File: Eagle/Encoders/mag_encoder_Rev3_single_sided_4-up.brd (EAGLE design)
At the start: 10 x 24 mm, 5 parts, among them IC1 A1203LH

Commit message: Updated ecoder gcode again...
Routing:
- net VCC: track 33.2 -> 36.7 mm
- net SIG: track 22.0 -> 24.4 mm
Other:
- board size 10 x 24 mm -> 12.9 x 24 mm
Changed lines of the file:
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@@
 <text x="11.8225" y="18.705" size="0.762" layer="25">SIG</text>
 <text x="8.838" y="18.705" size="0.762" layer="25">VCC</text>
-<wire x1="4.75" y1="1.5" x2="4.75" y2="25.5" width="0" layer="20"/>
-<wire x1="14.75" y1="25.5" x2="14.75" y2="1.5" width="0" layer="20"/>
-<wire x1="14.75" y1="1.5" x2="4.75" y2="1.5" width="0" layer="20"/>
-<wire x1="4.75" y1="25.5" x2="14.75" y2="25.5" width="0" layer="20"/>
+<wire x1="3.125" y1="1.5" x2="3.125" y2="25.5" width="0.01" layer="20"/>
+<wire x1="16" y1="25.5" x2="16" y2="1.5" width="0.01" layer="20"/>
+<wire x1="16" y1="1.5" x2="3.125" y2="1.5" width="0.01" layer="20"/>
+<wire x1="3.125" y1="25.5" x2="16" y2="25.5" width="0.01" layer="20"/>
 </plain>
 <attributes>
@@
 <contactref element="C1" pad="2"/>
 <contactref element="U$1" pad="P$3"/>
-<wire x1="12.375" y1="11.125" x2="9.875" y2="11.125" width="0.635" layer="1"/>
-<wire x1="9.875" y1="11.125" x2="7.75" y2="11.125" width="0.635" layer="1"/>
 <wire x1="7.75" y1="11.125" x2="7.667" y2="11.04" width="0.635" layer="1"/>
 <wire x1="12.375" y1="11.125" x2="12.412" y2="11.04" width="0.635" layer="1"/>
-<wire x1="9.875" y1="11.125" x2="9.875" y2="6.125" width="0.635" layer="1"/>
 <wire x1="9.875" y1="6.125" x2="9.852" y2="6.115" width="0.635" layer="1"/>
-<wire x1="7.375" y1="11.125" x2="7.375" y2="22" width="0.635" layer="1"/>
 <wire x1="7.375" y1="22" x2="7.2935" y2="22.0995" width="0.635" layer="1"/>
 <wire x1="7.375" y1="11.125" x2="7.667" y2="11.04" width="0.635" layer="1"/>
 <polygon width="0.4064" layer="1" thermals="no">
-<vertex x="-1" y="30.875"/>
-<vertex x="20.125" y="30.875"/>
-<vertex x="20.125" y="0.25"/>
-<vertex x="-0.625" y="0.25"/>
+<vertex x="2.125" y="26"/>
+<vertex x="16.625" y="26"/>
+<vertex x="16.625" y="0.25"/>
+<vertex x="2.25" y="0.25"/>
 </polygon>
+<wire x1="9.875" y1="6.125" x2="9.875" y2="10.25" width="1.016" layer="1"/>
+<wire x1="9.875" y1="10.25" x2="10.665" y2="11.04" width="1.016" layer="1"/>
+<wire x1="10.665" y1="11.04" x2="12.412" y2="11.04" width="1.016" layer="1"/>
+<wire x1="9.875" y1="10.25" x2="9.085" y2="11.04" width="1.016" layer="1"/>
+<wire x1="9.085" y1="11.04" x2="7.667" y2="11.04" width="1.016" layer="1"/>
+<wire x1="7.375" y1="11.125" x2="7.375" y2="22.018" width="1.016" layer="1"/>
+<wire x1="7.375" y1="22.018" x2="7.2935" y2="22.0995" width="1.016" layer="1"/>
 </signal>
 <signal name="VCC">
@@
 <contactref element="R1" pad="2"/>
 <contactref element="U$1" pad="P$2"/>
-<wire x1="7.75" y1="4.625" x2="7.75" y2="9.25" width="0.635" layer="1"/>
-<wire x1="8.75" y1="3.625" x2="7.75" y2="4.625" width="0.635" layer="1"/>
 <wire x1="7.75" y1="9.25" x2="7.667" y2="9.34" width="0.635" layer="1"/>
 <wire x1="8.75" y1="3.625" x2="8.752" y2="3.515" width="0.635" layer="1"/>
-<wire x1="9.375" y1="21.625" x2="9.375" y2="15.75" width="0.635" layer="1"/>
-<wire x1="9.75" y1="22" x2="9.375" y2="21.625" width="0.635" layer="1"/>
-<wire x1="9.375" y1="15.75" x2="9.252" y2="15.63" width="0.635" layer="1"/>
-<wire x1="9.75" y1="22" x2="9.7935" y2="22.0995" width="0.635" layer="1"/>
-<wire x1="6.75" y1="9.5" x2="7.375" y2="9.5" width="0.635" layer="1"/>
-<wire x1="5.625" y1="10.625" x2="6.75" y2="9.5" width="0.635" layer="1"/>
-<wire x1="5.625" y1="23" x2="5.625" y2="10.625" width="0.635" layer="1"/>
-<wire x1="6.375" y1="23.75" x2="5.625" y2="23" width="0.635" layer="1"/>
-<wire x1="8.375" y1="23.75" x2="6.375" y2="23.75" width="0.635" layer="1"/>
-<wire x1="9.75" y1="22.375" x2="8.375" y2="23.75" width="0.635" layer="1"/>
-<wire x1="7.375" y1="9.5" x2="7.667" y2="9.34" width="0.635" layer="1"/>
 <wire x1="9.75" y1="22.375" x2="9.7935" y2="22.0995" width="0.635" layer="1"/>
+<wire x1="8.75" y1="3.625" x2="7.667" y2="4.708" width="1.016" layer="1"/>
+<wire x1="7.667" y1="4.708" x2="7.667" y2="7.458" width="1.016" layer="1"/>
+<wire x1="7.667" y1="7.458" x2="7.667" y2="9.34" width="1.016" layer="1"/>
+<wire x1="8.375" y1="24.125" x2="9.7935" y2="22.7065" width="1.016" layer="1"/>
+<wire x1="9.7935" y1="22.7065" x2="9.7935" y2="22.0995" width="1.016" layer="1"/>
+<wire x1="4.5" y1="10.625" x2="7.667" y2="7.458" width="1.016" layer="1"/>
+<wire x1="4.5" y1="10.625" x2="4.5" y2="22.125" width="1.016" layer="1"/>
+<wire x1="4.5" y1="22.125" x2="6.5" y2="24.125" width="1.016" layer="1"/>
+<wire x1="6.5" y1="24.125" x2="8.375" y2="24.125" width="1.016" layer="1"/>
+<wire x1="9.252" y1="15.63" x2="9.25" y2="15.632" width="1.016" layer="1"/>
+<wire x1="9.25" y1="15.632" x2="9.25" y2="17.875" width="1.016" layer="1"/>
+<wire x1="9.25" y1="17.875" x2="9.7935" y2="18.4185" width="1.016" layer="1"/>
+<wire x1="9.7935" y1="18.4185" x2="9.7935" y2="22.0995" width="1.016" layer="1"/>
 </signal>
 <signal name="SIG">
@@
 <contactref element="C2" pad="1"/>
 <contactref element="U$1" pad="P$1"/>
-<wire x1="12.375" y1="5" x2="12.375" y2="9.25" width="0.635" layer="1"/>
-<wire x1="11" y1="3.625" x2="12.375" y2="5" width="0.635" layer="1"/>
 <wire x1="12.375" y1="9.25" x2="12.412" y2="9.34" width="0.635" layer="1"/>
 <wire x1="11" y1="3.625" x2="10.952" y2="3.515" width="0.635" layer="1"/>
-<wire x1="11" y1="20.75" x2="11" y2="15.75" width="0.635" layer="1"/>
-<wire x1="12.25" y1="22" x2="11" y2="20.75" width="0.635" layer="1"/>
 <wire x1="11" y1="15.75" x2="10.952" y2="15.63" width="0.635" layer="1"/>
 <wire x1="12.25" y1="22" x2="12.2935" y2="22.0995" width="0.635" layer="1"/>
-<wire x1="13.375" y1="9.5" x2="12.625" y2="9.5" width="0.635" layer="1"/>
-<wire x1="13.875" y1="10" x2="13.375" y2="9.5" width="0.635" layer="1"/>
-<wire x1="13.875" y1="12.625" x2="13.875" y2="10" width="0.635" layer="1"/>
-<wire x1="11.125" y1="15.375" x2="13.875" y2="12.625" width="0.635" layer="1"/>
-<wire x1="12.625" y1="9.5" x2="12.412" y2="9.34" width="0.635" layer="1"/>
 <wire x1="11.125" y1="15.375" x2="10.952" y2="15.63" width="0.635" layer="1"/>
+<wire x1="11" y1="3.625" x2="12.412" y2="5.037" width="1.016" layer="1"/>
+<wire x1="12.412" y1="5.037" x2="12.412" y2="7.75" width="1.016" layer="1"/>
+<wire x1="12.412" y1="7.75" x2="12.412" y2="9.34" width="1.016" layer="1"/>
+<wire x1="11" y1="15.75" x2="12.2935" y2="17.0435" width="1.016" layer="1"/>
+<wire x1="12.2935" y1="17.0435" x2="12.2935" y2="22.0995" width="1.016" layer="1"/>
+<wire x1="11.125" y1="15.375" x2="14.875" y2="11.625" width="1.016" layer="1"/>
+<wire x1="14.875" y1="11.625" x2="14.875" y2="9.75" width="1.016" layer="1"/>
+<wire x1="14.875" y1="9.75" x2="12.875" y2="7.75" width="1.016" layer="1"/>
+<wire x1="12.875" y1="7.75" x2="12.412" y2="7.75" width="1.016" layer="1"/>
 </signal>
 </signals>

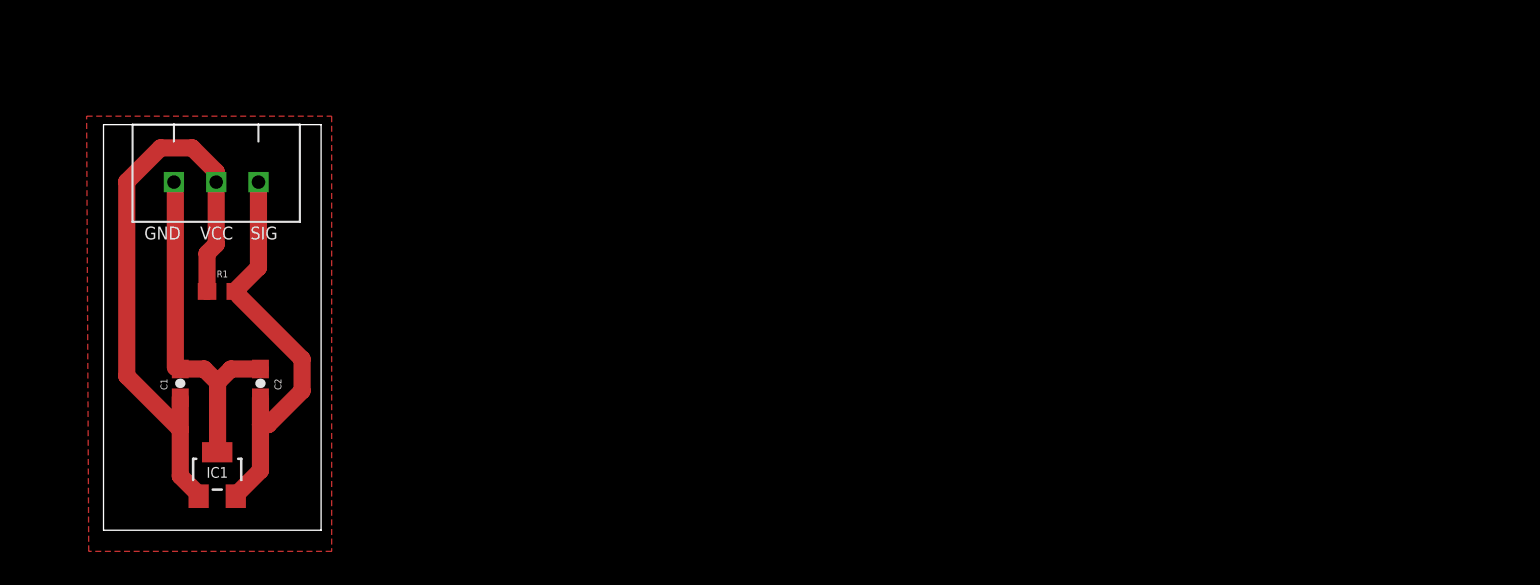
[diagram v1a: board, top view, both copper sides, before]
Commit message: Made changes to single-sided encoder boards and updated gcode that works for Lawlor's CNC router.
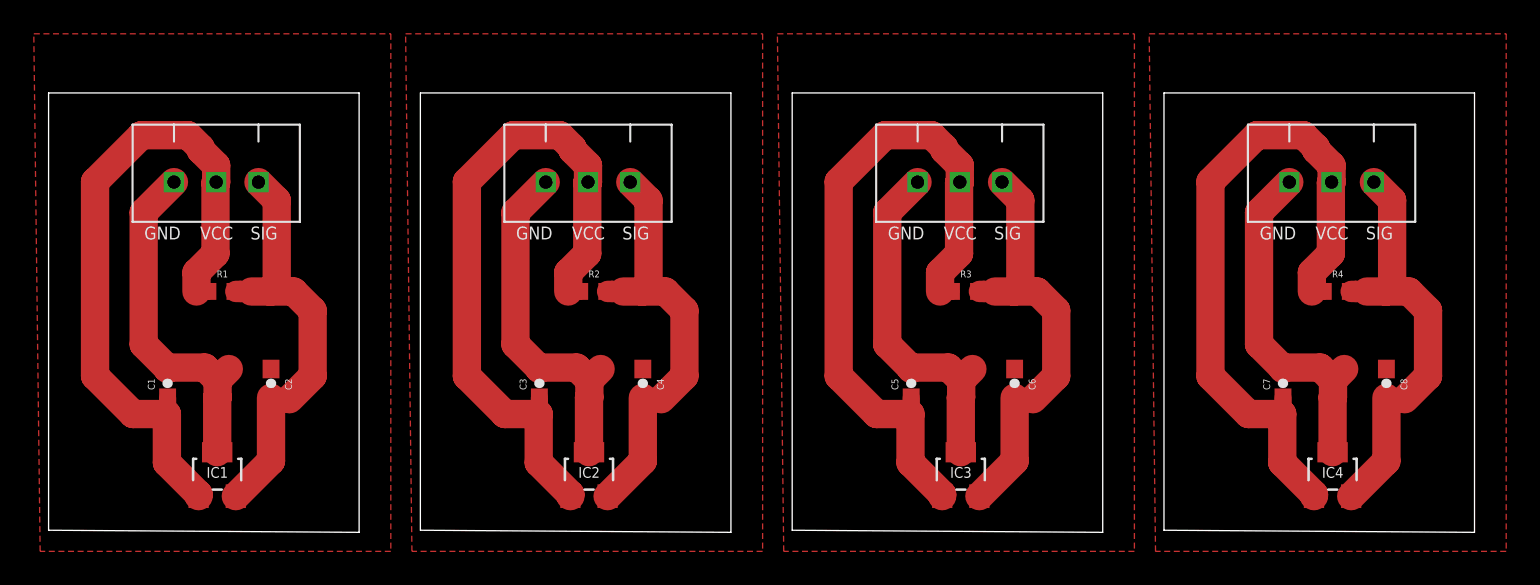
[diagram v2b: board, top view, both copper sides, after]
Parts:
- added C3, C5, C7: 100nF, SparkFun-Capacitors:0603-CAP
- added C4, C6, C8: 4.7nF, SparkFun-Capacitors:0603-CAP
- added IC2, IC3, IC4: A1203LH, allegro:SOT23-W
- added R2, R3, R4: 10k, SparkFun-Resistors:0603
- added U$2, U$3, U$4: 3_PIN_JST-XH, Clayton:3_PIN_JST-XH
- moved C1 0.75 mm to (6.92, 10.2)
- moved C2 0.62 mm to (13.0, 10.2)
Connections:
- new net GND1: C3.2, C4.2, IC2.3, U$2.P$3
- new net GND2: C5.2, C6.2, IC3.3, U$3.P$3
- new net GND3: C7.2, C8.2, IC4.3, U$4.P$3
- new net SIG1: C4.1, IC2.2, R2.1, U$2.P$1
- new net SIG2: C6.1, IC3.2, R3.1, U$3.P$1
- new net SIG3: C8.1, IC4.2, R4.1, U$4.P$1
- new net VCC1: C3.1, IC2.1, R2.2, U$2.P$2
- new net VCC2: C5.1, IC3.1, R3.2, U$3.P$2
- new net VCC3: C7.1, IC4.1, R4.2, U$4.P$2
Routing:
- net VCC2: track 0.00 -> 41.0 mm
- net VCC1: track 0.00 -> 41.0 mm
- net VCC3: track 0.00 -> 41.0 mm
- net SIG3: track 0.00 -> 26.0 mm
- net SIG2: track 0.00 -> 26.0 mm
- net SIG1: track 0.00 -> 26.0 mm
- net GND2: track 0.00 -> 20.9 mm
- net GND1: track 0.00 -> 20.9 mm
- net GND3: track 0.00 -> 20.9 mm
- net VCC: track 36.7 -> 41.0 mm
- net SIG: track 24.4 -> 26.0 mm
- added copper zone on layer 1, net GND1
- added copper zone on layer 1, net GND2
- added copper zone on layer 1, net GND3
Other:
- board size 12.9 x 24 mm -> 84.4 x 26 mm
